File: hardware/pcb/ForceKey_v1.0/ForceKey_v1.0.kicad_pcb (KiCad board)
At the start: 2 copper layers, 18 parts, among them CN1 PJ-320A, J1 PINHD_1x2_Male, J2 PINHD_1x4_Male, J3 PINHD_1x4_Male, Q1 BC817-40W, Q2 BC817-40W, Q3 BC817-40W, U1 PY32F002AL15S6TU, U2 ME6211C33M5, U3 PJ4054B

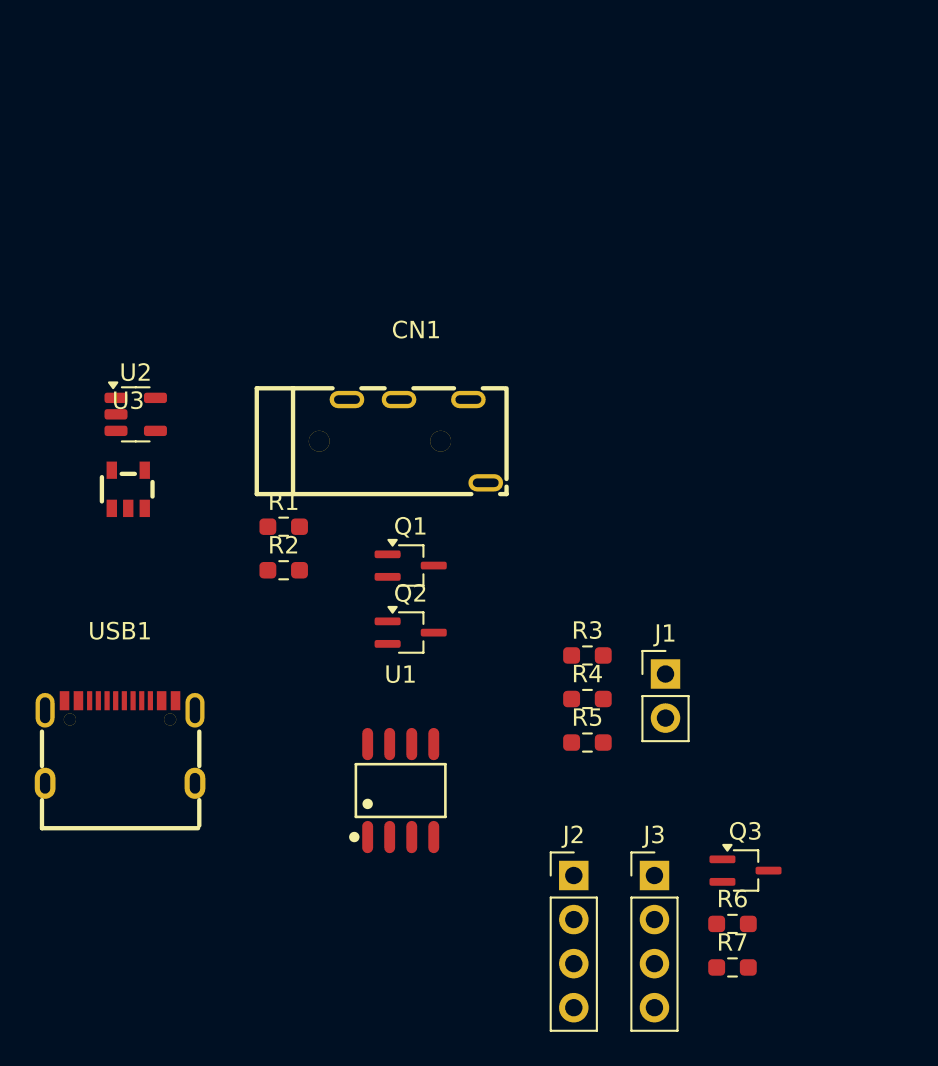
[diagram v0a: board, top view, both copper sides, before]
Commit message: added switch & basic PCB layout draft
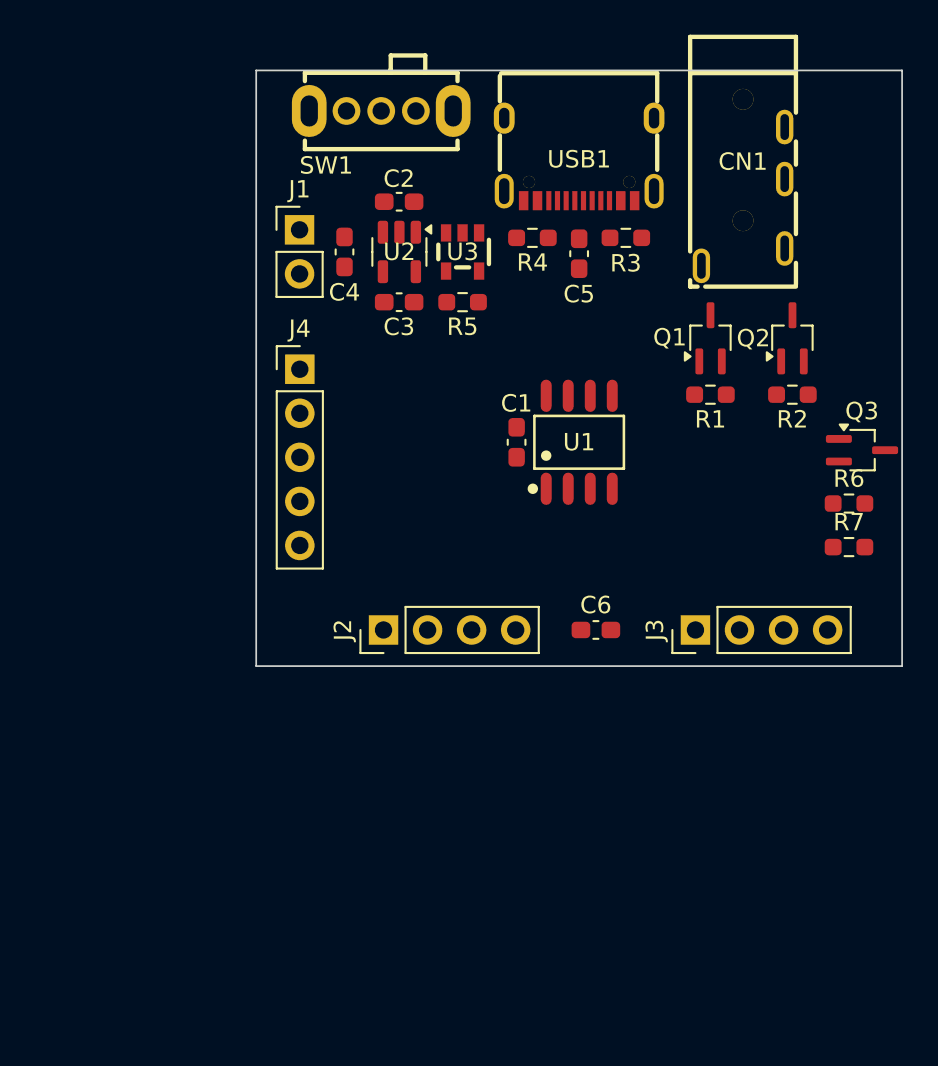
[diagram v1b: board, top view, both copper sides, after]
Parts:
- added C1: 1u, Capacitor_SMD:C_0603_1608Metric_Pad1.08x0.95mm_HandSolder, F.Cu at (122.0, 56.9)
- added C2: 1u, Capacitor_SMD:C_0603_1608Metric_Pad1.08x0.95mm_HandSolder, F.Cu at (115.2, 43.1)
- added C3: 1u, Capacitor_SMD:C_0603_1608Metric_Pad1.08x0.95mm_HandSolder, F.Cu at (115.2, 48.9)
- added C4: 10u, Capacitor_SMD:C_0603_1608Metric_Pad1.08x0.95mm_HandSolder, F.Cu at (112.1, 46.0)
- added C5: 10u, Capacitor_SMD:C_0603_1608Metric_Pad1.08x0.95mm_HandSolder, F.Cu at (125.6, 46.1)
- added C6: 10u, Capacitor_SMD:C_0603_1608Metric_Pad1.08x0.95mm_HandSolder, F.Cu at (126.5, 67.8)
- added J4: PINHD_1x5_Male, Connector_PinHeader_2.54mm:PinHeader_1x05_P2.54mm_Vertical, F.Cu at (109.5, 52.7)
- added SW1: SK12D07VG6, SK12D07VG6:SW-TH_SK12D07VG6, F.Cu at (114.2, 37.8)
- R1, R2: value 470 -> 2k
- R5: value 2.5k -> 2k
- R6: value 470 -> 5.1k
- R7: value 1k -> 5.1k
- moved USB1 42.8 mm to (125.6, 40.6), turned to 180 degrees
- moved J1 33.2 mm to (109.5, 44.7)
- moved R2 31.0 mm to (137.9, 54.2), turned to 180 degrees
- moved Q2 27.8 mm to (137.9, 51.0), turned to 90 degrees
- moved R4 26.8 mm to (122.9, 45.2), turned to 180 degrees
- moved R5 26.4 mm to (118.9, 48.9)
- moved R1 25.8 mm to (133.1, 54.2), turned to 180 degrees
- moved R7 25.1 mm to (141.1, 63.0)
- moved R6 25.1 mm to (141.1, 60.5)
- moved Q3 25.1 mm to (141.9, 57.4)
- moved R3 24.2 mm to (128.3, 45.2)
- moved U3 23.6 mm to (118.9, 46.0), turned to 180 degrees
- moved CN1 23.5 mm to (135.0, 42.8), turned to -90 degrees
- moved U1 22.6 mm to (125.6, 56.9)
- moved Q1 21.7 mm to (133.2, 51.0), turned to 90 degrees
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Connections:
- CN1 pad 2: Net-(CN1-Pad2) -> Net-(Q3-B)
- R1 pad 1: unconnected-(R1-Pad1) -> /DOT
- R2 pad 1: unconnected-(R2-Pad1) -> /DASH
- R6 pad 2: Net-(CN1-Pad2) -> VBat
- R7 pad 1: Net-(Q3-B) -> /LDO_EN
- U1 pad 4: unconnected-(U1-PA14-SWC/PB3-Pad4) -> /DASH
- U1 pad 5: unconnected-(U1-PA13-SWD-Pad5) -> /DOT
- U1 pad 6: unconnected-(U1-PA2/PF2-NRST-Pad6) -> /RST
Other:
- board outline added: 37.2 x 34.3 mm

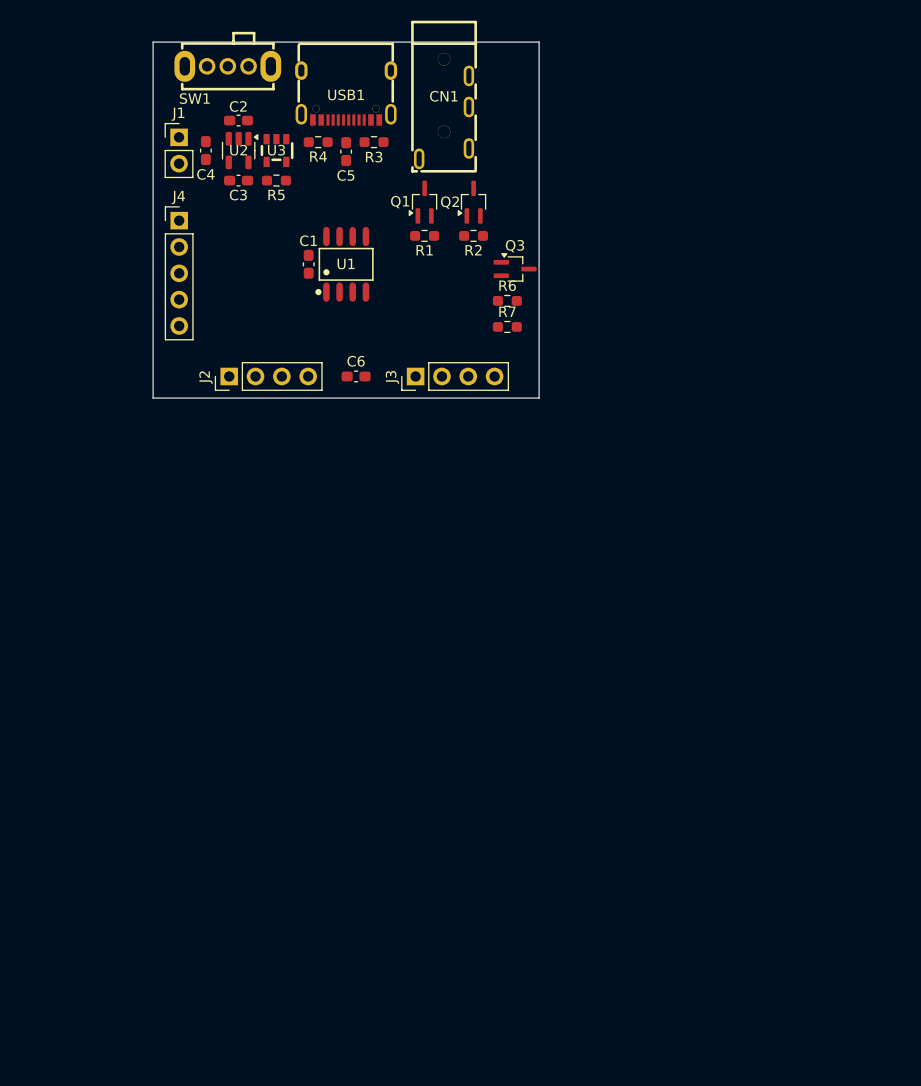
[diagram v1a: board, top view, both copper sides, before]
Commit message: added power traces, updated footprints
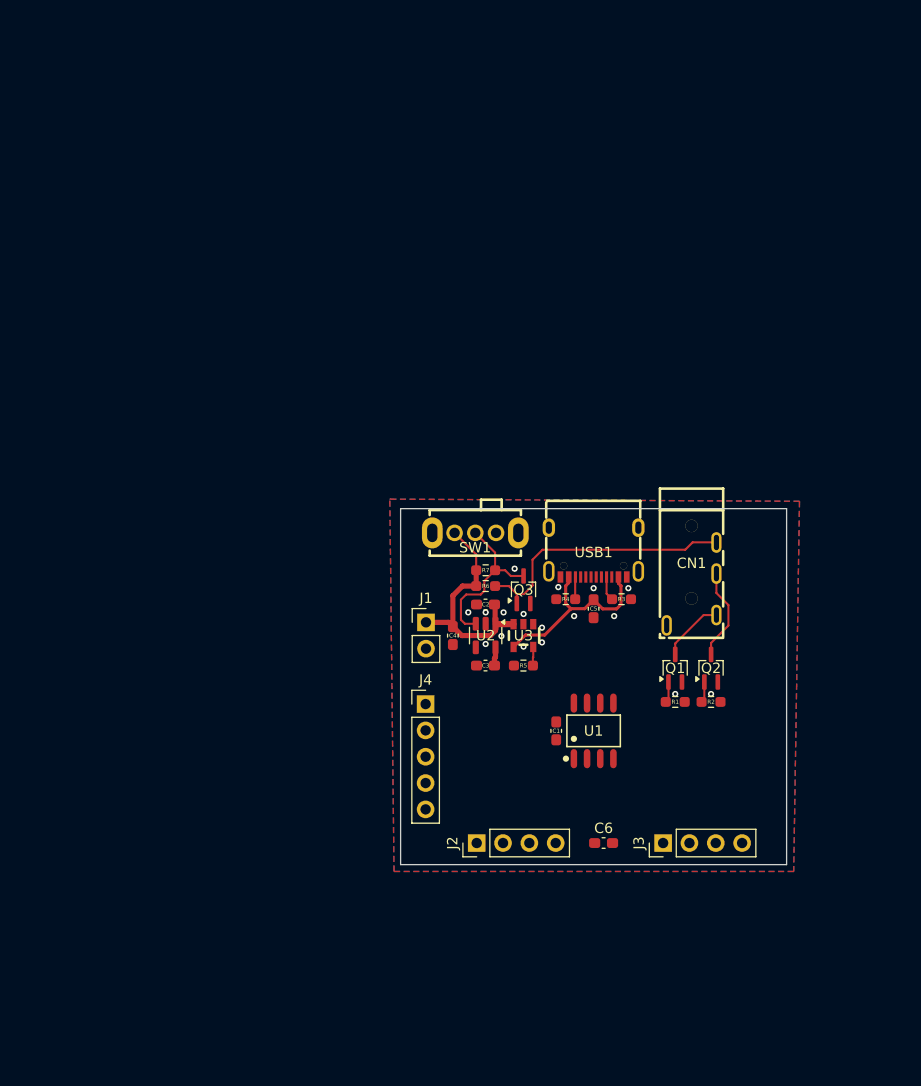
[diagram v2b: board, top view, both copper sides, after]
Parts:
- moved C3 52.5 mm to (139.0, 95.7)
- moved C4 52.5 mm to (135.9, 92.8)
- moved R5 52.5 mm to (142.7, 95.7)
- moved U2 52.5 mm to (139.0, 92.8)
- moved U3 52.5 mm to (142.7, 92.8)
- moved J1 52.5 mm to (133.3, 91.5)
- moved C2 52.4 mm to (139.0, 89.8)
- moved J4 52.3 mm to (133.2, 99.4)
- moved R1 51.0 mm to (157.3, 99.2)
- moved Q1 51.0 mm to (157.3, 95.9)
- moved C1 50.9 mm to (145.8, 102.0)
- moved C6 50.9 mm to (150.4, 112.8)
- moved CN1 50.9 mm to (158.9, 87.8)
- moved J3 50.9 mm to (156.2, 112.8)
- moved SW1 50.9 mm to (138.0, 82.9)
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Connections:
- SW1 pad 1: VBat -> GND
- SW1 pad 3: GND -> VBat
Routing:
- net Net-(Q3-B): track 0.00 -> 26.1 mm
- net VBat: track 0.00 -> 23.1 mm
- net VUSB: track 0.00 -> 18.9 mm
- net /LDO_EN: track 0.00 -> 15.9 mm
- net Net-(Q2-C): track 0.00 -> 8.97 mm
- net Net-(Q1-C): track 0.00 -> 6.17 mm
- net Net-(USB1-CC1): track 0.00 -> 2.36 mm
- net Net-(USB1-CC2): track 0.00 -> 2.15 mm
- net Net-(Q2-B): track 0.00 -> 2.03 mm
- net Net-(Q1-B): track 0.00 -> 2.03 mm
- net Net-(U3-PROG): track 0.00 -> 1.81 mm
- net +3.3V: track 0.00 -> 1.80 mm
- net GND: vias 0 -> 17
- added copper zone on B.Cu, net GND
- added copper zone on F.Cu, net GND

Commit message: updated PCB
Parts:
- added H1: MountingHole_3.2mm_M3_DIN965_Pad, MountingHole:MountingHole_3.2mm_M3_DIN965_Pad, F.Cu at (129.5, 85.7)
- added H2: MountingHole_3.2mm_M3_DIN965_Pad, MountingHole:MountingHole_3.2mm_M3_DIN965_Pad, F.Cu at (169.5, 85.7)
- added H3: MountingHole_3.2mm_M3_DIN965_Pad, MountingHole:MountingHole_3.2mm_M3_DIN965_Pad, F.Cu at (129.5, 115.7)
- added H4: MountingHole_3.2mm_M3_DIN965_Pad, MountingHole:MountingHole_3.2mm_M3_DIN965_Pad, F.Cu at (169.5, 115.7)
- moved Q1 2.61 mm to (159.9, 95.9)
- moved R1 2.61 mm to (159.9, 99.2)
- moved CN1 2.61 mm to (161.5, 87.8)
- moved Q2 2.61 mm to (163.4, 95.9)
- moved R2 2.61 mm to (163.4, 99.2)
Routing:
- net Net-(Q3-B): track 26.1 -> 28.7 mm
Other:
- board size 37.2 x 34.3 mm -> 50 x 40 mm

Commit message: Finished Schematic and PCB
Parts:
- added REF**: KiCad-Logo2_5mm_Copper, Symbol:KiCad-Logo2_5mm_Copper, F.Cu at (146.5, 115.8)
- added REF**: OSHW-Logo2_7.3x6mm_Copper, Symbol:OSHW-Logo2_7.3x6mm_Copper, F.Cu at (135.6, 115.8)
- added REF**: OSHW-Logo2_7.3x6mm_SilkScreen, Symbol:OSHW-Logo2_7.3x6mm_SilkScreen, F.Cu at (135.6, 115.8)
- added REF**: KiCad-Logo2_5mm_SilkScreen, Symbol:KiCad-Logo2_5mm_SilkScreen, F.Cu at (146.5, 115.8)
- added REF**: KiCad-Logo2_5mm_SilkScreen, Symbol:KiCad-Logo2_5mm_SilkScreen, B.Cu at (152.3, 115.8)
- added REF**: OSHW-Logo2_7.3x6mm_SilkScreen, Symbol:OSHW-Logo2_7.3x6mm_SilkScreen, B.Cu at (163.2, 115.9)
- added REF**: OSHW-Logo2_7.3x6mm_Copper, Symbol:OSHW-Logo2_7.3x6mm_Copper, B.Cu at (163.2, 115.9)
- added REF**: KiCad-Logo2_5mm_Copper, Symbol:KiCad-Logo2_5mm_Copper, B.Cu at (152.3, 115.8)
- J4: value PINHD_1x5_Male -> Conn_ARM_SWD_TagConnect_TC2030-NL; footprint Connector_PinHeader_2.54mm:PinHeader_1x05_P2.54mm_Vertical -> Connector:Tag-Connect_TC2030-IDC-NL_2x03_P1.27mm_Vertical
- moved J2 28.6 mm to (165.4, 103.9), turned to -90 degrees
- moved J4 24.1 mm to (156.0, 91.4), turned to -90 degrees
- moved J3 17.4 mm to (141.2, 103.9), turned to -90 degrees
- moved C1 9.34 mm to (149.5, 93.3), turned to 0 degrees
- moved C6 8.97 mm to (149.5, 103.9)
- moved U1 5.01 mm to (149.5, 96.9), turned to -90 degrees
- moved R2 3.61 mm to (159.8, 98.9)
- moved Q2 3.61 mm to (159.8, 95.7)
- moved R1 3.27 mm to (163.2, 98.9)
- moved Q1 3.27 mm to (163.2, 95.7)
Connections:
- J2 pad 2: unconnected-(J2-Pad2) -> /SCK
- J2 pad 3: unconnected-(J2-Pad3) -> /LEFT_DIO
- J3 pad 2: unconnected-(J3-Pad2) -> /SCK
- J3 pad 3: unconnected-(J3-Pad3) -> /RIGHT_DIO
- J4 pad 3: /DASH -> /RST
- J4 pad 4: /RST -> /RIGHT_DIO
- U1 pad 2: unconnected-(U1-PA4/PA10-Pad2) -> /SCK
- U1 pad 3: unconnected-(U1-PA3-Pad3) -> /LEFT_DIO
- U1 pad 4: /DASH -> /RIGHT_DIO
- U1 pad 7: unconnected-(U1-PA1-Pad7) -> /DASH
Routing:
- net +3.3V: track 1.80 -> 73.3 mm
- net /SCK: track 0.00 -> 37.1 mm
- net /RIGHT_DIO: track 0.00 -> 32.6 mm
- net /DOT: track 0.00 -> 27.0 mm
- net /LEFT_DIO: track 0.00 -> 20.5 mm
- net /DASH: track 0.00 -> 13.5 mm
- net /RST: track 0.00 -> 8.53 mm
- net Net-(Q1-C): track 6.17 -> 3.75 mm
- net Net-(Q2-C): track 8.97 -> 9.98 mm
- net VUSB: track 18.9 -> 18.1 mm
- net GND: vias 17 -> 46
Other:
- board text added: "Force Key"
- board text added: "Frédéric Druppel ON4PFD 10-2024 fredcorp.cc"
- board text added: "a Solid State Paddle clone (Original design by 9A5N, redesigned by ON4PFD)"
